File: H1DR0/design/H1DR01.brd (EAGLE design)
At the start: 34.6 x 30 mm, 28 parts, among them P1 HEXABIT_17.32_NO_P6, U1 STM32G0B1CEU6QFN_B1CEU6_STM-L, U2 MAX3232CSE, X1 XTALL_CSTCE8M00G52

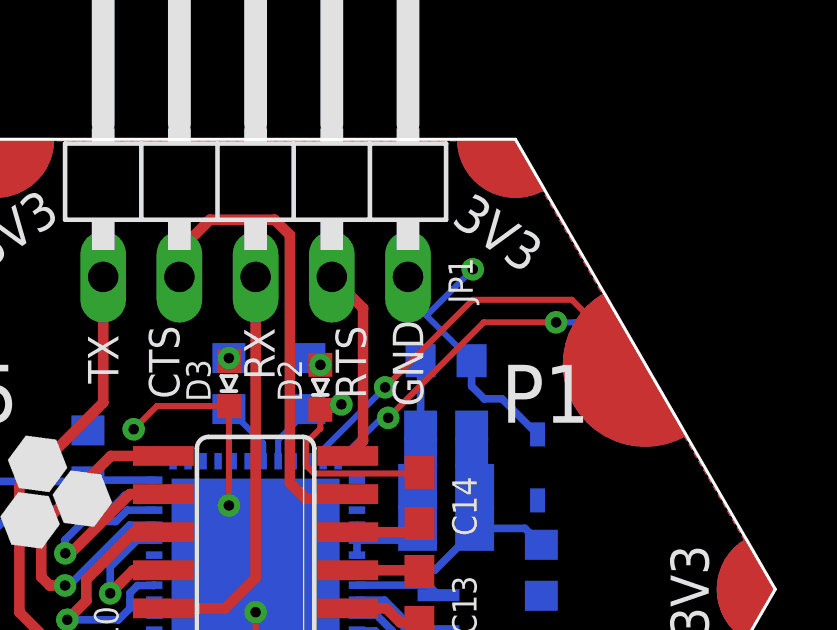
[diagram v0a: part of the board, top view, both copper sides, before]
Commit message: - Fixed layout - Fixed descriptions in BOM
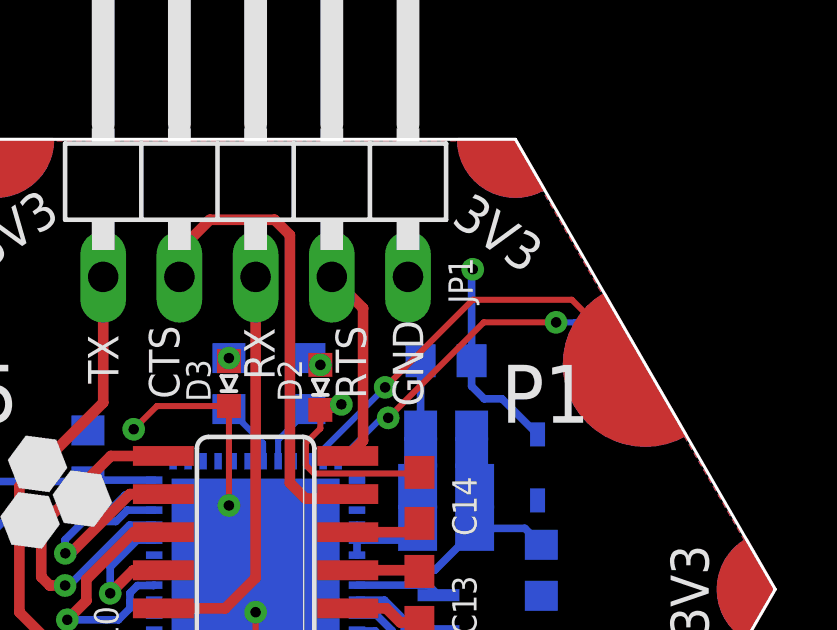
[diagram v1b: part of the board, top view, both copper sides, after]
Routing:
- net VDD: track 8.02 -> 6.78 mm
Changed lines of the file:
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@@
 <drawing>
 <settings>
-<setting alwaysvectorfont="yes"/>
+<setting alwaysvectorfont="no"/>
 <setting verticaltext="up"/>
 </settings>
-<grid distance="5" unitdist="mil" unit="mil" style="lines" multiple="1" display="yes" altdistance="5" altunitdist="mil" altunit="mil"/>
+<grid distance="6.25" unitdist="mil" unit="mil" style="lines" multiple="1" display="yes" altdistance="5" altunitdist="mil" altunit="mil"/>
 <layers>
 <layer number="1" name="Top" color="4" fill="1" visible="yes" active="yes"/>
@@
 <wire x1="42.291" y1="41.021" x2="41.871" y2="41.441" width="0.254" layer="16"/>
 <wire x1="41.871" y1="41.441" x2="41.871" y2="42.291" width="0.254" layer="16"/>
-<wire x1="41.871" y1="42.291" x2="40.3665" y2="43.7955" width="0.2032" layer="16"/>
-<wire x1="40.3665" y1="43.7955" x2="41.91" y2="45.339" width="0.2032" layer="16"/>
 <via x="41.91" y="45.339" extent="1-16" drill="0.35"/>
 <contactref element="C11" pad="1"/>
+<wire x1="41.871" y1="42.291" x2="41.871" y2="45.3" width="0.254" layer="16"/>
+<wire x1="41.871" y1="45.3" x2="41.91" y2="45.339" width="0.254" layer="16"/>
 </signal>
 <signal name="UART1_CTS">

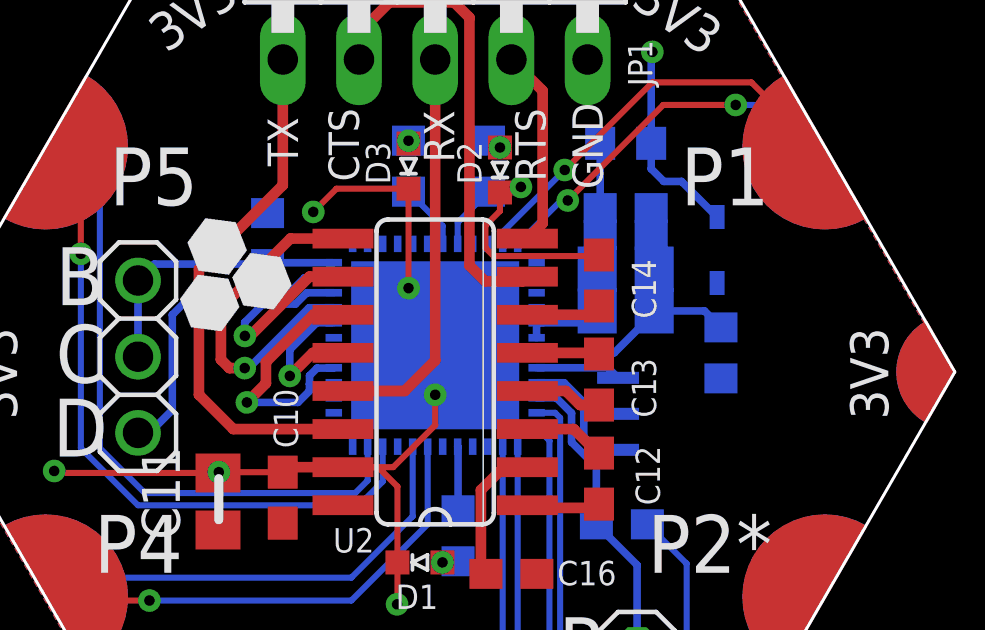
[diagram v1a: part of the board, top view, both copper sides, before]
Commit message: - Changed logo in layout - Rearranged components in BOM
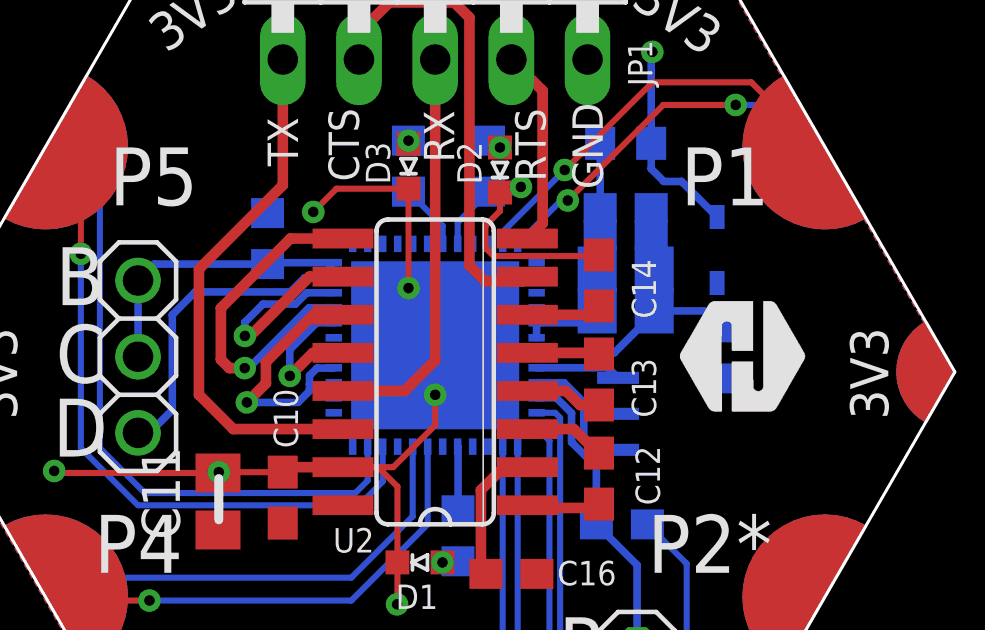
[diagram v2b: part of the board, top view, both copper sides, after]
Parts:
- added U$1: (no value), HEXABITZ_USER_INTERFACE_PARTS:HEXA-LOGO
